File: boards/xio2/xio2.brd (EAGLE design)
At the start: 170 x 100 mm, 376 parts, among them J1 12401598E4#2A, Q1 BSS138, Q2 BSS138, Q3 BC817-16LT3G, Q4 BC817-16LT3G, Y2 FA-238 25.0000MB-K3

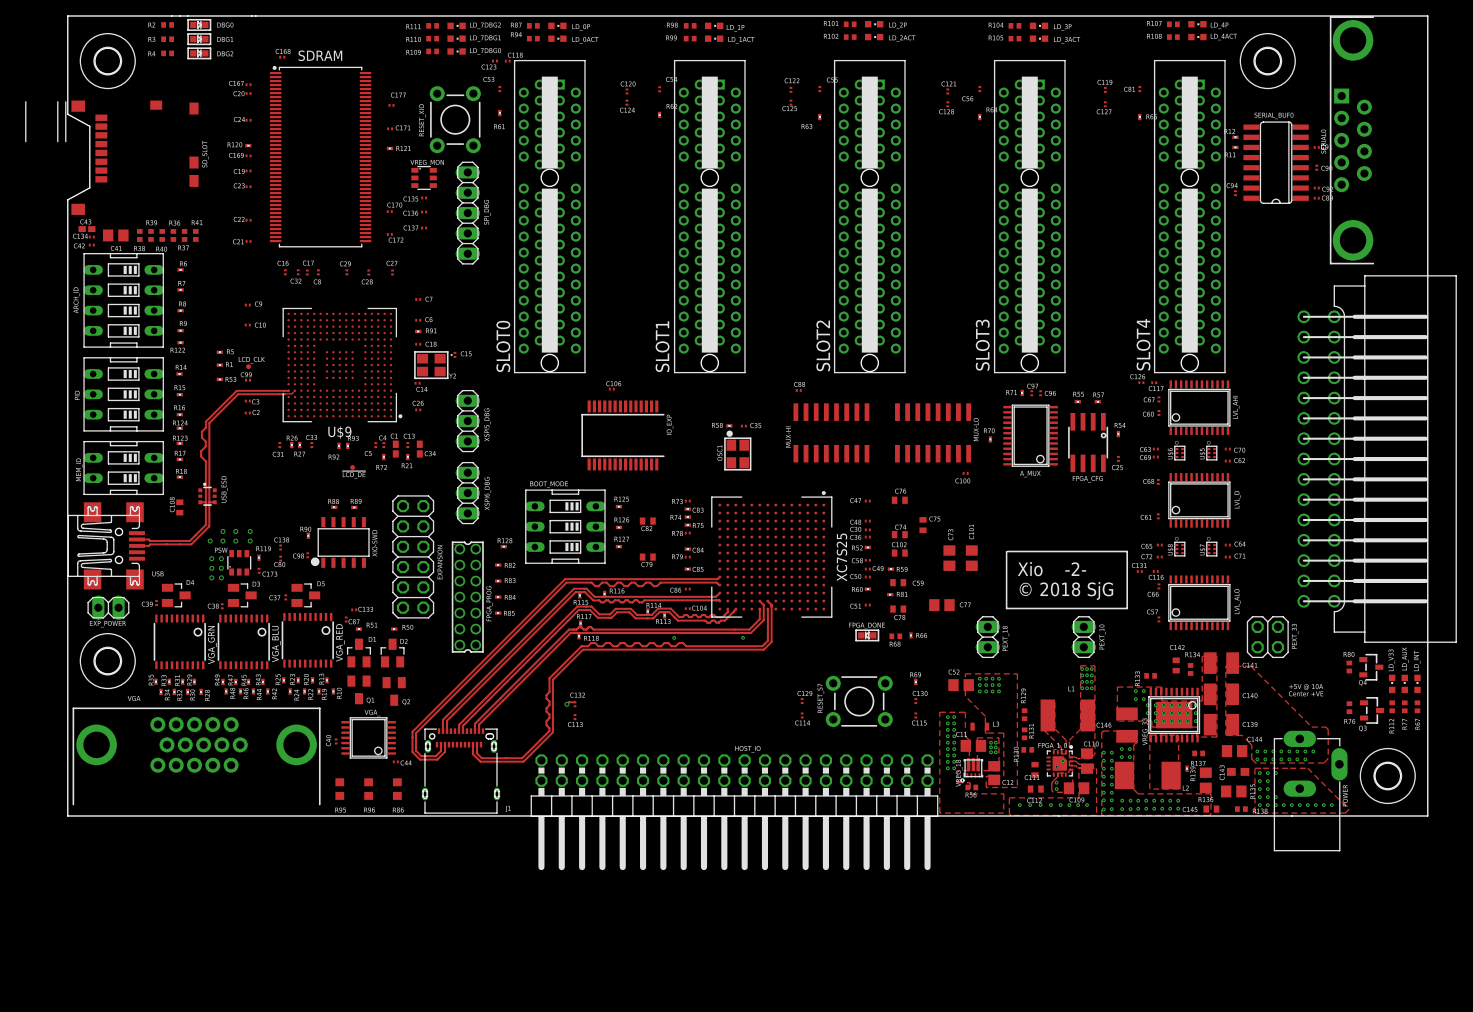
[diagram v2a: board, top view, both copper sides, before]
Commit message: Route the XIO_USB_{P,N} now that the STM32 chip is rotated
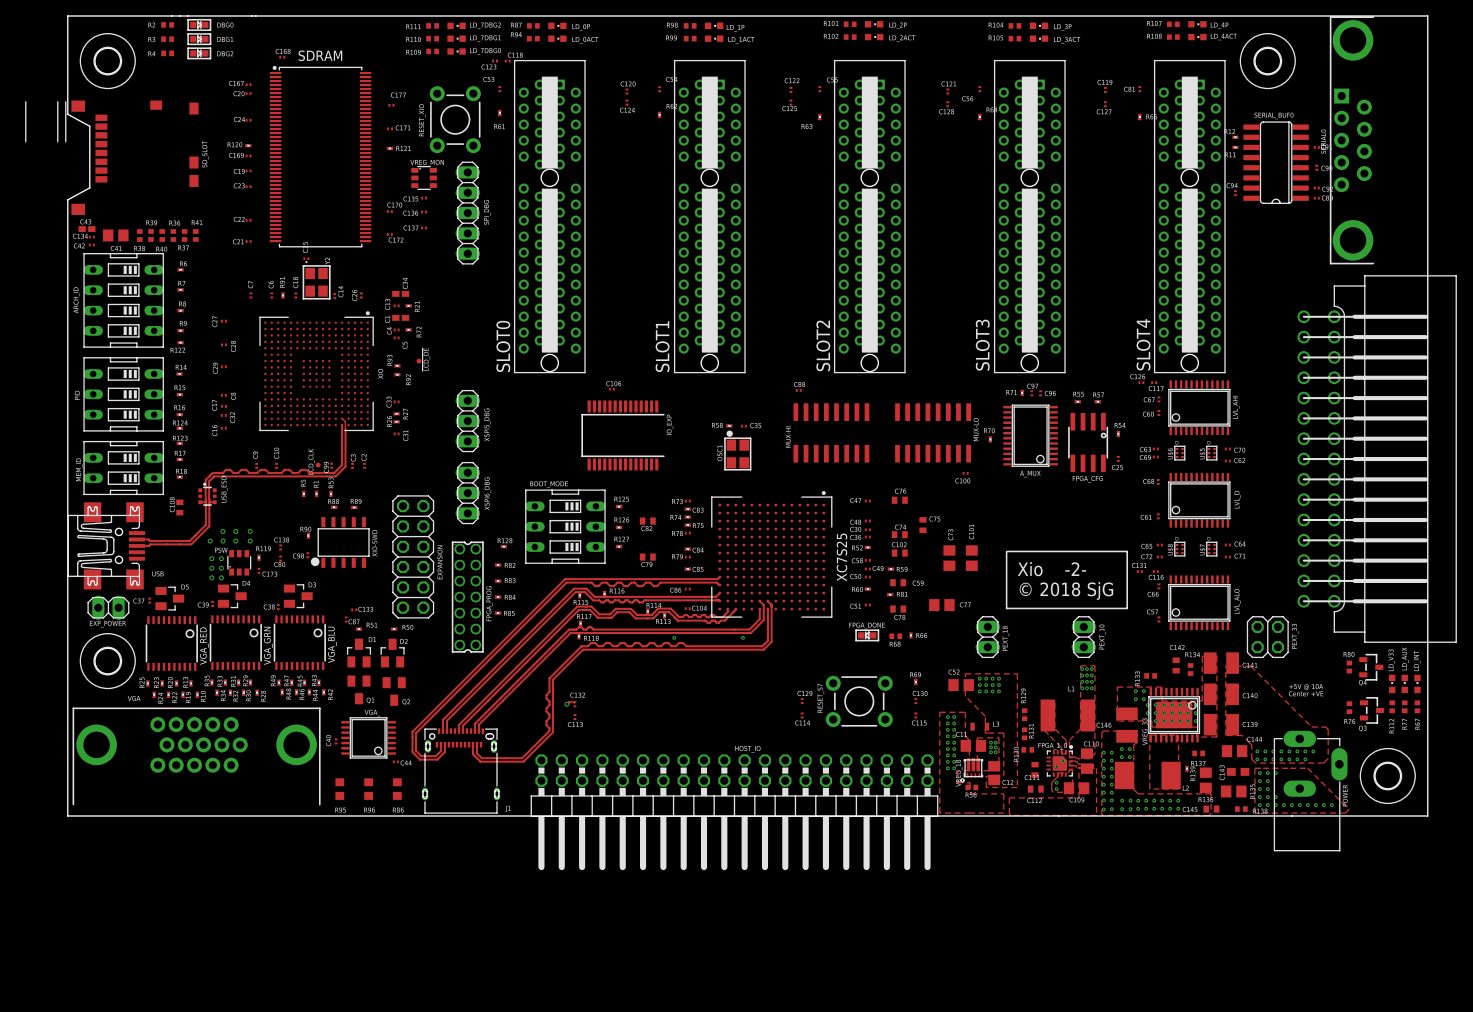
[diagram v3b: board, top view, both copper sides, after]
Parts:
- removed U$9: STM32H743-XIO, sjg-stm32:BGA289C80P17X17_1400X1400X110
- added XIO: STM32H743-XIO, sjg-stm32:BGA289C80P17X17_1400X1400X110
- moved C15 22.1 mm to (29.8, 70.3), turned to 180 degrees
- moved C27 21.9 mm to (19.5, 62.5), turned to 180 degrees
- moved C16 21.0 mm to (19.5, 49.1), turned to 180 degrees
- moved C7 20.9 mm to (22.9, 65.7), turned to 90 degrees
- moved R5 20.6 mm to (29.5, 40.9), turned to 90 degrees
- moved C28 20.2 mm to (19.5, 59.5), turned to 180 degrees
- moved C32 20.2 mm to (19.5, 50.7), turned to 180 degrees
- moved R1 20.1 mm to (31.1, 40.9), turned to 270 degrees
- moved C9 20.1 mm to (23.6, 44.4), turned to 270 degrees
- moved R53 19.9 mm to (32.9, 40.9), turned to 90 degrees
- moved C17 19.7 mm to (19.5, 51.8), turned to 180 degrees
- moved C34 19.5 mm to (41.6, 65.9), turned to 0 degrees
- moved C29 19.4 mm to (19.5, 56.8), turned to 180 degrees
- moved C8 19.4 mm to (19.5, 53.2), turned to 180 degrees
- moved R21 18.9 mm to (42.6, 64.4), turned to 0 degrees
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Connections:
- net !ADDR_VALID_READ!: now also XIO.M2; no longer U$9.M2
- net !ADDR_VALID_WRITE!: now also XIO.M3; no longer U$9.M3
- net !IO_EXP_IRQ!: now also XIO.D3; no longer U$9.D3
- net !IO_EXP_SEL!: now also XIO.N2; no longer U$9.N2
- net !RESET!: now also XIO.K1; no longer U$9.K1
- net !SDRAM_CAS!: now also XIO.D6; no longer U$9.D6
- net !SDRAM_RAS!: now also XIO.T7; no longer U$9.T7
- net !SDRAM_WE!: now also XIO.P4; no longer U$9.P4
- net !SPI_IRQ!: now also XIO.D2; no longer U$9.D2
- net +3V3: now also XIO.A6, XIO.B1, XIO.C17, XIO.E11, XIO.E6, XIO.E9, XIO.F17, XIO.F5, XIO.G13, XIO.G5, XIO.H13, XIO.H5, XIO.J13, XIO.K13, XIO.K5, XIO.L13, XIO.L5, XIO.M13, XIO.M5, XIO.N10, XIO.N11, XIO.N12, XIO.N7, XIO.N8, XIO.P17, XIO.U12; no longer U$9.A6, U$9.B1, U$9.C17, U$9.E11, U$9.E6, U$9.E9, U$9.F17, U$9.F5, U$9.G13, U$9.G5, U$9.H13, U$9.H5, U$9.J13, U$9.K13, U$9.K5, U$9.L13, U$9.L5, U$9.M13, U$9.M5, U$9.N10, U$9.N11, U$9.N12, U$9.N7, U$9.N8, U$9.P17, U$9.U12
- net AGND: now also XIO.N1, XIO.P1; no longer U$9.N1, U$9.P1
- net BOOT0: now also XIO.E8; no longer U$9.E8
- net GND: now also XIO.A1, XIO.A17, XIO.B2, XIO.B6, XIO.C10, XIO.C13, XIO.C16, XIO.F1, XIO.F2, XIO.G10, XIO.G11, XIO.G16, XIO.G2, XIO.G7, XIO.G8, XIO.G9, XIO.H10, XIO.H11, XIO.H7, XIO.H8, XIO.H9, XIO.J10, XIO.J11, XIO.J16, XIO.J17, XIO.J3, XIO.J7, XIO.J8, XIO.J9, XIO.K10, XIO.K11, XIO.K15, XIO.K7, XIO.K8, XIO.K9, XIO.L10, XIO.L11, XIO.L15, XIO.L7, XIO.L8, XIO.L9, XIO.M15, XIO.N16, XIO.R4, XIO.R8, XIO.T12, XIO.U1, XIO.U17; no longer U$9.A1, U$9.A17, U$9.B2, U$9.B6, U$9.C10, U$9.C13, U$9.C16, U$9.F1, U$9.F2, U$9.G10, U$9.G11, U$9.G16, U$9.G2, U$9.G7, U$9.G8, U$9.G9, U$9.H10, U$9.H11, U$9.H7, U$9.H8, U$9.H9, U$9.J10, U$9.J11, U$9.J16, U$9.J17, U$9.J3, U$9.J7, U$9.J8, U$9.J9, U$9.K10, U$9.K11, U$9.K15, U$9.K7, U$9.K8, U$9.K9, U$9.L10, U$9.L11, U$9.L15, U$9.L7, U$9.L8, U$9.L9, U$9.M15, U$9.N16, U$9.R4, U$9.R8, U$9.T12, U$9.U1, U$9.U17
- net HOST_A0: now also XIO.U5; no longer U$9.U5
- net HOST_A1: now also XIO.T5; no longer U$9.T5
- net HOST_A10: now also XIO.P11; no longer U$9.P11
- net HOST_A11: now also XIO.P12; no longer U$9.P12
- net HOST_A12: now also XIO.T14; no longer U$9.T14
- net HOST_A13: now also XIO.U14; no longer U$9.U14
- net HOST_A14: now also XIO.U15; no longer U$9.U15
- net HOST_A15: now also XIO.T15; no longer U$9.T15
- net HOST_A2: now also XIO.R6; no longer U$9.R6
- net HOST_A3: now also XIO.C6; no longer U$9.C6
- net HOST_A4: now also XIO.B7; no longer U$9.B7
- net HOST_A5: now also XIO.A5; no longer U$9.A5
- net HOST_A6: now also XIO.B5; no longer U$9.B5
- net HOST_A7: now also XIO.C5; no longer U$9.C5
- net HOST_A8: now also XIO.D5; no longer U$9.D5
- net HOST_A9: now also XIO.D4; no longer U$9.D4
- net LCDCLK: now also XIO.F16; no longer U$9.F16
- net LCD_B0: now also XIO.D11; no longer U$9.D11
- net LCD_B1: now also XIO.E10; no longer U$9.E10
- net LCD_B2: now also XIO.D10; no longer U$9.D10
- net LCD_B3: now also XIO.B10; no longer U$9.B10
- net LCD_B4: now also XIO.C8; no longer U$9.C8
- net LCD_B5: now also XIO.B8; no longer U$9.B8
- net LCD_B6: now also XIO.A8; no longer U$9.A8
- net LCD_B7: now also XIO.C7; no longer U$9.C7
- net LCD_G0: now also XIO.N14; no longer U$9.N14
- net LCD_G1: now also XIO.N13; no longer U$9.N13
- net LCD_G2: now also XIO.M14; no longer U$9.M14
- net LCD_G3: now also XIO.L14; no longer U$9.L14
- net LCD_G4: now also XIO.K14; no longer U$9.K14
- net LCD_G5: now also XIO.J14; no longer U$9.J14
- net LCD_G6: now also XIO.J15; no longer U$9.J15
- net LCD_G7: now also XIO.H17; no longer U$9.H17
- net LCD_HS: now also XIO.H1; no longer U$9.H1
- net LCD_R0: now also XIO.P5; no longer U$9.P5
- net LCD_R1: now also XIO.N6; no longer U$9.N6
- net LCD_R2: now also XIO.P6; no longer U$9.P6
- net LCD_R3: now also XIO.T6; no longer U$9.T6
- net LCD_R4: now also XIO.U6; no longer U$9.U6
- net LCD_R5: now also XIO.U7; no longer U$9.U7
- net LCD_R6: now also XIO.R12; no longer U$9.R12
- net LCD_R7: now also XIO.N15; no longer U$9.N15
- net LCD_VS: now also XIO.H2; no longer U$9.H2
- net MCU_CTS: now also XIO.B12; no longer U$9.B12
- net MCU_RTS: now also XIO.A12; no longer U$9.A12
- net MCU_RX: now also XIO.B11; no longer U$9.B11
- net MCU_TX: now also XIO.A11; no longer U$9.A11
- net N$1: now also XIO.A14; no longer U$9.A14
- net N$13: now also XIO.R15; no longer U$9.R15
- net N$14: now also XIO.R16; no longer U$9.R16
- net N$15: now also XIO.R17; no longer U$9.R17
- net N$53: now also XIO.D7; no longer U$9.D7
- net N$57: now also XIO.C3; no longer U$9.C3
- net N$61: now also XIO.E5; no longer U$9.E5
- net N$65: now also XIO.C11; no longer U$9.C11
- net PDR_ON: now also XIO.E7; no longer U$9.E7
- net SD0: now also XIO.E13; no longer U$9.E13
- net SD1: now also XIO.E14; no longer U$9.E14
- net SD2: now also XIO.A13; no longer U$9.A13
- net SD3: now also XIO.B13; no longer U$9.B13
- net SDCD: now also XIO.E3; no longer U$9.E3
- net SDCLK: now also XIO.C12; no longer U$9.C12
- net SDCMD: now also XIO.D12; no longer U$9.D12
- net SDRAM_A0: now also XIO.G4; no longer U$9.G4
- net SDRAM_A1: now also XIO.G3; no longer U$9.G3
- net SDRAM_A10: now also XIO.T8; no longer U$9.T8
- net SDRAM_A11: now also XIO.U8; no longer U$9.U8
- net SDRAM_A12: now also XIO.H16; no longer U$9.H16
- net SDRAM_A2: now also XIO.G1; no longer U$9.G1
- net SDRAM_A3: now also XIO.H4; no longer U$9.H4
- net SDRAM_A4: now also XIO.J5; no longer U$9.J5
- net SDRAM_A5: now also XIO.J4; no longer U$9.J4
- net SDRAM_A6: now also XIO.R7; no longer U$9.R7
- net SDRAM_A7: now also XIO.P7; no longer U$9.P7
- net SDRAM_A8: now also XIO.P8; no longer U$9.P8
- net SDRAM_A9: now also XIO.R9; no longer U$9.R9
- net SDRAM_BA0: now also XIO.H14; no longer U$9.H14
- net SDRAM_BA1: now also XIO.G14; no longer U$9.G14
- net SDRAM_CLK: now also XIO.F15; no longer U$9.F15
- net SDRAM_D0: now also XIO.P16; no longer U$9.P16
- net SDRAM_D1: now also XIO.P15; no longer U$9.P15
- net SDRAM_D10: now also XIO.T10; no longer U$9.T10
- net SDRAM_D11: now also XIO.U10; no longer U$9.U10
- net SDRAM_D12: now also XIO.R11; no longer U$9.R11
- net SDRAM_D13: now also XIO.U16; no longer U$9.U16
- net SDRAM_D14: now also XIO.T17; no longer U$9.T17
- net SDRAM_D15: now also XIO.T16; no longer U$9.T16
- net SDRAM_D16: now also XIO.T13; no longer U$9.T13
- net SDRAM_D17: now also XIO.R13; no longer U$9.R13
- net SDRAM_D18: now also XIO.P13; no longer U$9.P13
- net SDRAM_D19: now also XIO.P14; no longer U$9.P14
- net SDRAM_D2: now also XIO.D13; no longer U$9.D13
- net SDRAM_D20: now also XIO.R14; no longer U$9.R14
- net SDRAM_D21: now also XIO.D16; no longer U$9.D16
- net SDRAM_D22: now also XIO.B17; no longer U$9.B17
- net SDRAM_D23: now also XIO.B16; no longer U$9.B16
- net SDRAM_D24: now also XIO.A16; no longer U$9.A16
- net SDRAM_D25: now also XIO.A15; no longer U$9.A15
- net SDRAM_D26: now also XIO.B15; no longer U$9.B15
- net SDRAM_D27: now also XIO.C14; no longer U$9.C14
- net SDRAM_D28: now also XIO.A2; no longer U$9.A2
- net SDRAM_D29: now also XIO.B3; no longer U$9.B3
- net SDRAM_D3: now also XIO.E12; no longer U$9.E12
- net SDRAM_D30: now also XIO.E2; no longer U$9.E2
- net SDRAM_D31: now also XIO.F3; no longer U$9.F3
- net SDRAM_D4: now also XIO.U9; no longer U$9.U9
- net SDRAM_D5: now also XIO.T9; no longer U$9.T9
- net SDRAM_D6: now also XIO.P9; no longer U$9.P9
- net SDRAM_D7: now also XIO.N9; no longer U$9.N9
- net SDRAM_D8: now also XIO.P10; no longer U$9.P10
- net SDRAM_D9: now also XIO.R10; no longer U$9.R10
- net SDRAM_DQM0: now also XIO.C4; no longer U$9.C4
- net SDRAM_DQM1: now also XIO.B4; no longer U$9.B4
- net SDRAM_DQM2: now also XIO.A4; no longer U$9.A4
- net SDRAM_DQM3: now also XIO.A3; no longer U$9.A3
- net SPI_IRQ0: now also XIO.H15; no longer U$9.H15
- net SPI_IRQ1: now also XIO.G15; no longer U$9.G15
- net SPI_IRQ2: now also XIO.A10; no longer U$9.A10
- net SPI_IRQ3: now also XIO.A9; no longer U$9.A9
- net SPI_IRQ4: now also XIO.B9; no longer U$9.B9
- net SPI_MISO: now also XIO.D1; no longer U$9.D1
- net SPI_MUX_IN: now also XIO.P2; no longer U$9.P2
- net SPI_SS0: now also XIO.L2; no longer U$9.L2
- net SPI_SS1: now also XIO.T4; no longer U$9.T4
- net SPI_SS2: now also XIO.U4; no longer U$9.U4
- net SPI_SS3: now also XIO.C2; no longer U$9.C2
- net SPI_SS4: now also XIO.C1; no longer U$9.C1
- net STM_MUX_CTL: now also XIO.M4; no longer U$9.M4
- net STM_MUX_D0: now also XIO.N5; no longer U$9.N5
- net STM_MUX_D1: now also XIO.N4; no longer U$9.N4
- net STM_MUX_D2: now also XIO.N3; no longer U$9.N3
- net STM_MUX_D3: now also XIO.U2; no longer U$9.U2
- net STM_MUX_D4: now also XIO.U3; no longer U$9.U3
- net STM_MUX_D5: now also XIO.T3; no longer U$9.T3
- net STM_MUX_D6: now also XIO.R3; no longer U$9.R3
- net STM_MUX_D7: now also XIO.R5; no longer U$9.R5
- net XIO_CLK_IN: now also XIO.J1; no longer U$9.J1
- net XIO_CLK_OUT: now also XIO.J2; no longer U$9.J2
- net XIO_RX: now also XIO.F13; no longer U$9.F13
- net XIO_SWDCLK: now also XIO.B14; no longer U$9.B14
- net XIO_SWDIO: now also XIO.C15; no longer U$9.C15
- net XIO_TX: now also XIO.F14; no longer U$9.F14
- net XIO_USB_ID: now also XIO.D14; no longer U$9.D14
- net XIO_USB_N: now also XIO.E17; no longer U$9.E17
- net XIO_USB_P: now also XIO.E16; no longer U$9.E16
- net XIO_USB_VBUS: now also XIO.D15; no longer U$9.D15
- net XIO_VCAP1: now also XIO.U11; no longer U$9.U11
- net XIO_VCAP2: now also XIO.D17; no longer U$9.D17
- net XIO_VCAP3: now also XIO.A7; no longer U$9.A7
- net XIO_VDDA: now also XIO.L1, XIO.M1; no longer U$9.L1, U$9.M1
- net XSPI5_MISO_R: now also XIO.K4; no longer U$9.K4
- net XSPI5_MOSI: now also XIO.L4; no longer U$9.L4
- net XSPI5_SCK: now also XIO.K3; no longer U$9.K3
- net XSPI6_MISO: now also XIO.C9; no longer U$9.C9
- net XSPI6_MOSI_R: now also XIO.D8; no longer U$9.D8
- net XSPI6_SCK_R: now also XIO.D9; no longer U$9.D9
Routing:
- net XIO_USB_P: track 36.0 -> 40.4 mm
- net XIO_USB_N: track 36.0 -> 40.2 mm

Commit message: routed board
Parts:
- moved C99 0.40 mm to (33.0, 44.8)
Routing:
- net GND: track 0.00 -> 645.3 mm, vias 52 -> 362
- net HOST_A0: track 0.00 -> 405.4 mm, vias 0 -> 7
- net HOST_A11: track 0.00 -> 328.7 mm, vias 0 -> 7
- net HOST_A12: track 0.00 -> 318.0 mm, vias 0 -> 8
- net HOST_A2: track 0.00 -> 303.8 mm, vias 0 -> 6
- net HOST_A6: track 0.00 -> 303.2 mm, vias 0 -> 5
- net HOST_A7: track 0.00 -> 300.8 mm, vias 0 -> 5
- net HOST_A1: track 0.00 -> 294.3 mm, vias 0 -> 8
- net HOST_A9: track 0.00 -> 284.1 mm, vias 0 -> 9
- net HOST_A10: track 0.00 -> 280.2 mm, vias 0 -> 8
- net HOST_A5: track 0.00 -> 279.4 mm, vias 0 -> 4
- net HOST_A3: track 0.00 -> 278.3 mm, vias 0 -> 4
- net HOST_A4: track 0.00 -> 270.4 mm, vias 0 -> 5
- net MCU_CTS: track 0.00 -> 266.8 mm, vias 0 -> 3
- net HOST_A15: track 0.00 -> 265.1 mm, vias 0 -> 8
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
